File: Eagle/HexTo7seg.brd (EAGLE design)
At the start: 100 x 100 mm, 167 parts, among them CN2 1X04_SMD_STRAIGHT_COMBO

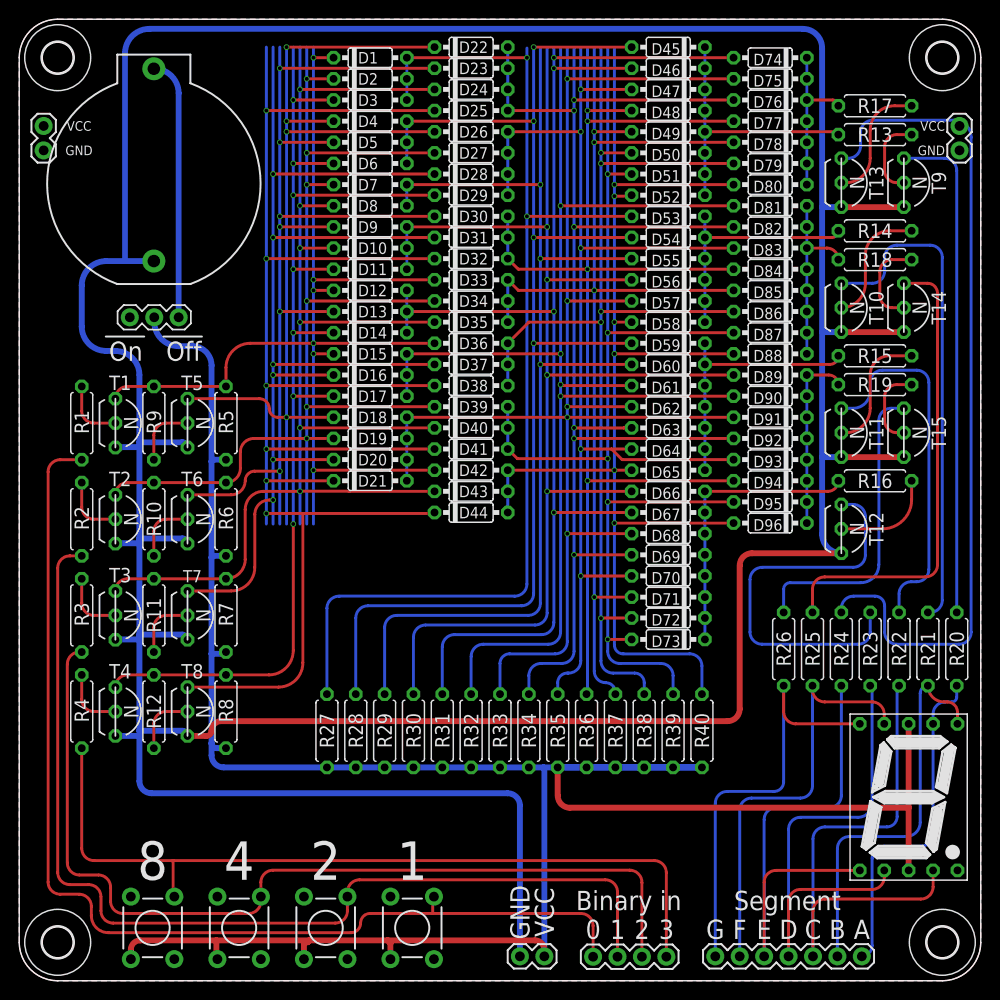
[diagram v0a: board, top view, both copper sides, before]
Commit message: Silk cleanup
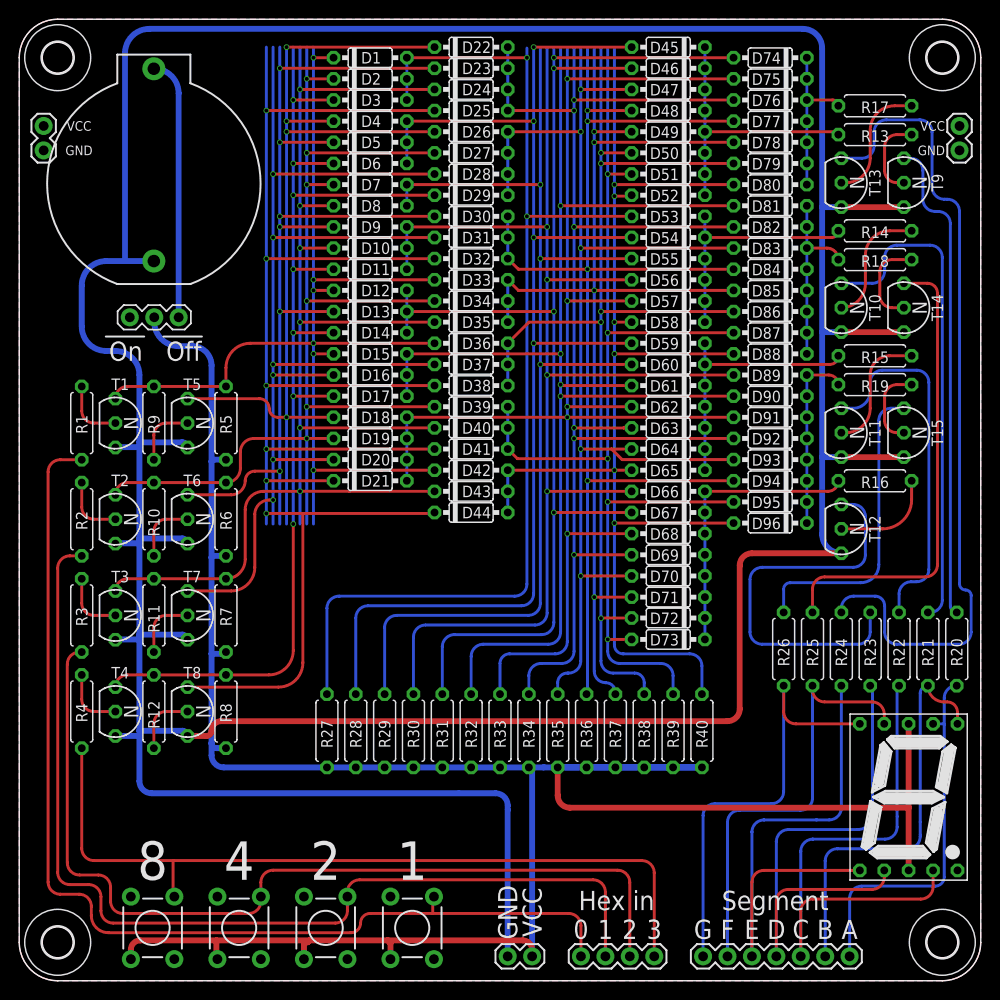
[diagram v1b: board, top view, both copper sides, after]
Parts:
- moved CN1 1.27 mm to (50.8, 2.54)
- moved CN3 1.27 mm to (86.4, 2.54)
- moved CN2 1.26 mm to (58.4, 2.54)
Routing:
- net N$2: track 35.0 -> 38.4 mm
- net N$11: track 52.8 -> 55.4 mm
- net N$12: track 52.9 -> 55.5 mm
- net N$10: track 55.6 -> 58.1 mm
- net SEGA: track 52.0 -> 50.1 mm
- net SEGE: track 86.8 -> 85.0 mm
- net N$9: track 40.9 -> 42.4 mm
- net VCC: track 249.0 -> 247.6 mm
- net IN1: track 106.2 -> 104.9 mm
- net IN3: track 84.8 -> 83.5 mm
- net IN2: track 96.7 -> 95.4 mm
- net IN0: track 112.5 -> 111.2 mm
- net GND: track 409.9 -> 408.7 mm
- net N$13: track 44.2 -> 45.5 mm
- net N$14: track 45.1 -> 46.2 mm
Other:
- board text added: "Hex in"
- board text removed: "Binary in"
